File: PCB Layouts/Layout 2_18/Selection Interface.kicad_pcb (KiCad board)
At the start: 4 copper layers, 110 x 90 mm, 95 parts

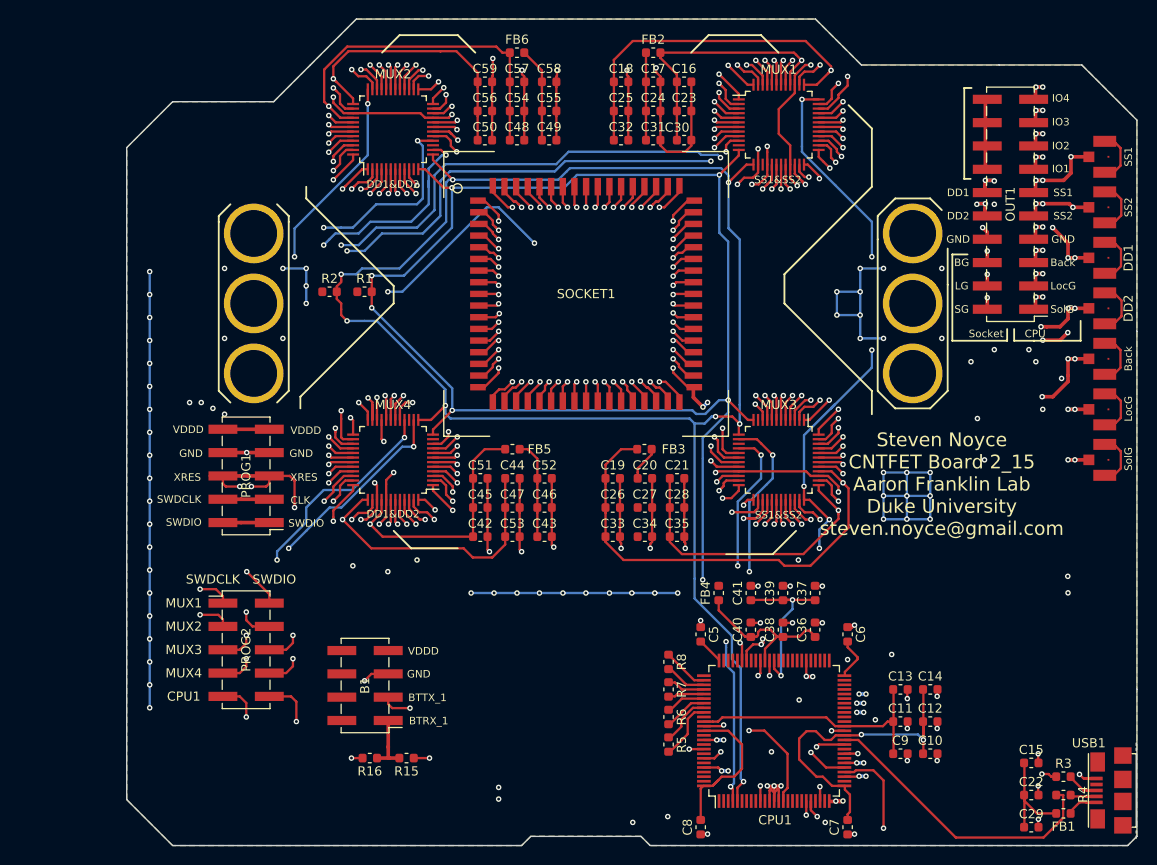
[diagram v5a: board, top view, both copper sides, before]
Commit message: Trying to clean up signal routing so that I can move PSoC chip up and to the right
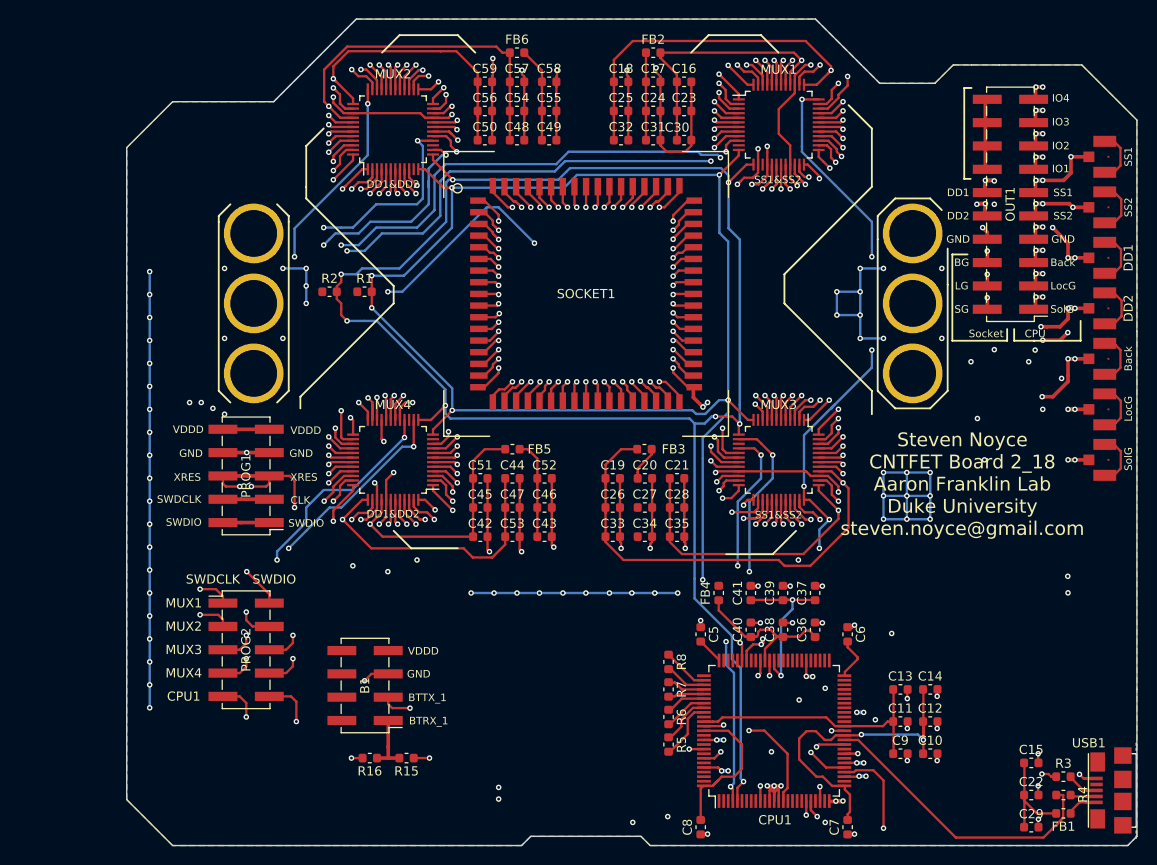
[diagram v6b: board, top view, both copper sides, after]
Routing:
- net DD2: track 263.1 -> 257.9 mm, vias 13 -> 12
- net DD1: track 262.9 -> 264.7 mm, vias 15 -> 13
- net IO4: track 87.3 -> 85.8 mm
- net IO3: track 87.5 -> 86.1 mm
- net SS1: track 163.6 -> 162.7 mm
- net IO2: track 78.8 -> 78.3 mm, vias 5 -> 4
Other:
- outline, holes or cut-outs redrawn
- board text added: "Steven Noyce CNTFET Board 2_18 Aaron Franklin Lab Duke University steven.noyce@gmail.com"
- board text removed: "Steven Noyce CNTFET Board 2_15 Aaron Franklin Lab Duke University steven.noyce@gmail.com"

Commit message: Moved the IO header down to clean up the top right corner of layout 2_18
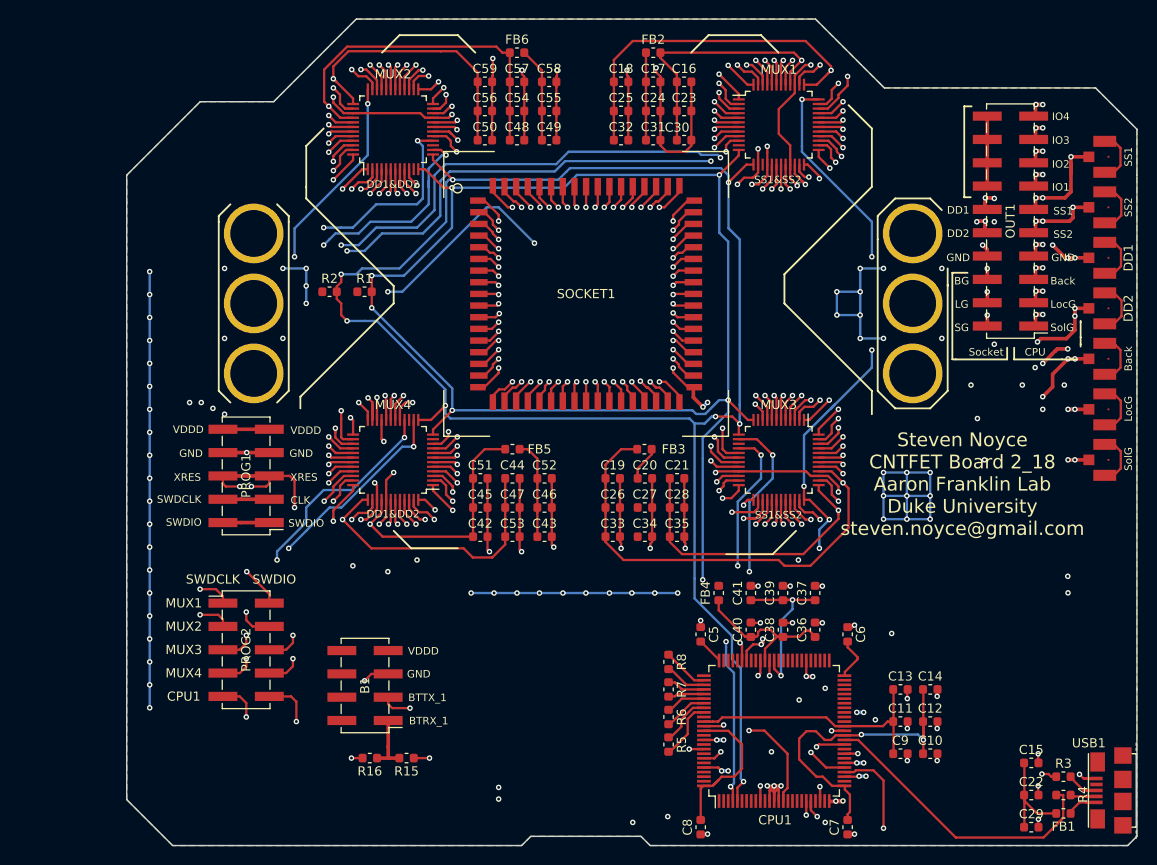
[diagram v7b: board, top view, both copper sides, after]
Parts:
- moved OUT1 1.83 mm to (246.2, 92.0)
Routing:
- net DD1: track 264.7 -> 260.5 mm
- net BackGate: track 77.0 -> 73.4 mm
- net BackGate_Socket: track 76.8 -> 74.3 mm
- net LocalGates: track 73.1 -> 71.0 mm
- net SS1: track 162.7 -> 164.7 mm
- net IO2: track 78.3 -> 76.4 mm
- net SolutionGate: track 74.3 -> 72.4 mm
- net IO4: track 85.8 -> 83.9 mm
- net IO1: track 78.7 -> 77.7 mm
- net IO3: track 86.1 -> 85.1 mm
- net SS2: track 156.1 -> 156.6 mm
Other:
- outline, holes or cut-outs redrawn

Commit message: Moved CPU1 up and to the right. Also moved the related power and capacitor circuitry. Re-routed all major analog signals. Left some digital signals unconnected because I need to start deciding where the external resistors and op-amps will be on board
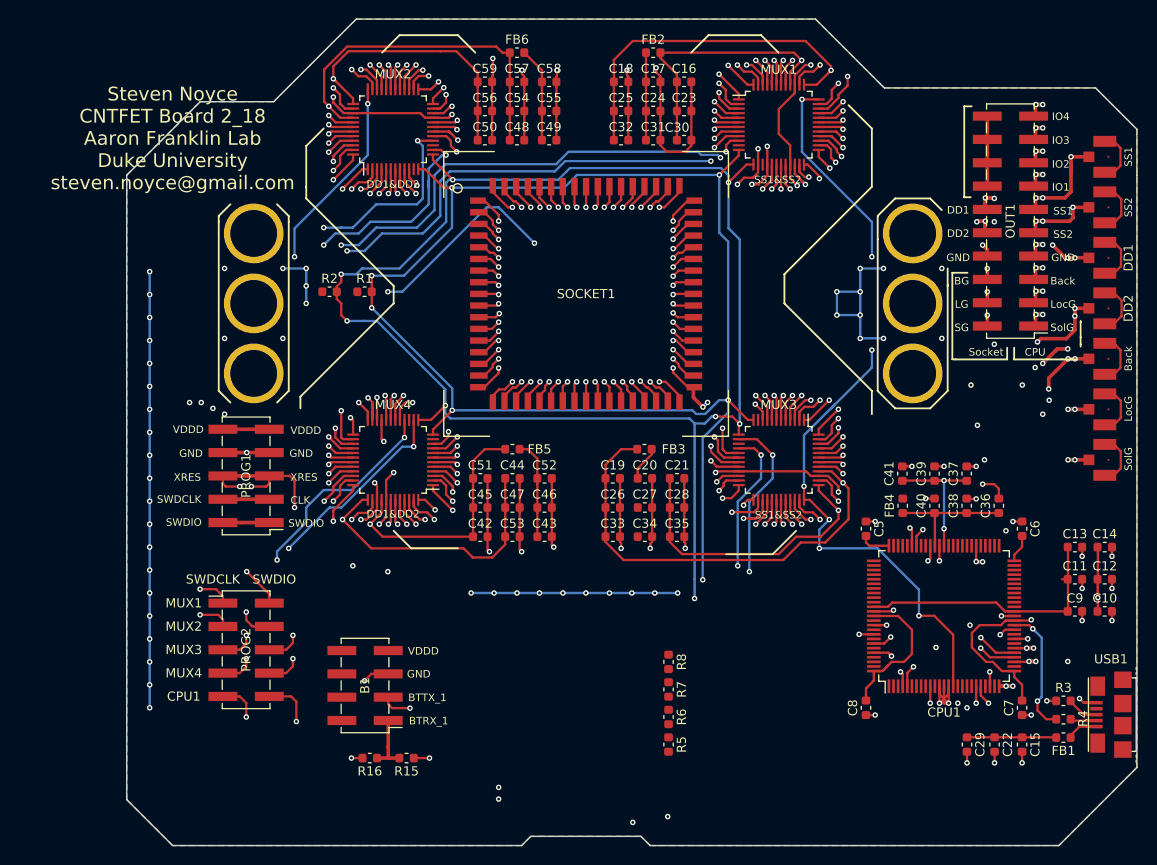
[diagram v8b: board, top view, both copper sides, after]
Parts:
- moved C10 24.5 mm to (256.5, 134.5)
- moved C11 24.5 mm to (253.2, 131.0)
- moved C12 24.5 mm to (256.5, 131.0)
- moved C13 24.5 mm to (253.2, 127.5)
- moved C14 24.5 mm to (256.5, 127.5)
- moved C9 24.5 mm to (253.2, 134.5)
- moved C36 24.1 mm to (245.0, 123.0)
- moved C38 24.1 mm to (241.5, 123.0)
- moved C40 24.1 mm to (238.0, 123.0)
- moved C7 23.0 mm to (247.5, 145.0)
- moved CPU1 22.3 mm to (239.0, 135.0)
- moved C6 22.2 mm to (247.5, 125.5)
- moved C8 22.2 mm to (230.5, 145.0)
- moved FB4 22.2 mm to (234.5, 123.0)
- moved C5 21.4 mm to (230.5, 125.5)
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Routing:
- net SS2: track 156.6 -> 120.7 mm, vias 9 -> 8
- net SS1: track 164.7 -> 132.0 mm, vias 10 -> 9
- net GND: track 327.1 -> 300.8 mm, vias 116 -> 106
- net I2C0_SCL: track 180.8 -> 156.7 mm, vias 9 -> 8
- net IO4: track 83.9 -> 60.0 mm, vias 4 -> 3
- net IO3: track 85.1 -> 62.1 mm
- net IO2: track 76.4 -> 53.8 mm
- net I2C0_SDA: track 188.2 -> 166.1 mm, vias 8 -> 9
- net SolutionGate: track 72.4 -> 52.2 mm
- net BackGate: track 73.4 -> 53.2 mm, vias 6 -> 5
- net USBDM_C1: track 33.0 -> 14.1 mm, vias 0 -> 2
- net DD2: track 258.1 -> 239.6 mm, vias 12 -> 10
- net USBDP_C1: track 31.4 -> 13.1 mm
- net IO1: track 77.7 -> 61.2 mm
- net LocalGates: track 71.0 -> 54.6 mm
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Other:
- outline, holes or cut-outs redrawn
